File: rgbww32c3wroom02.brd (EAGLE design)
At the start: 36.8 x 20.3 mm, 25 parts

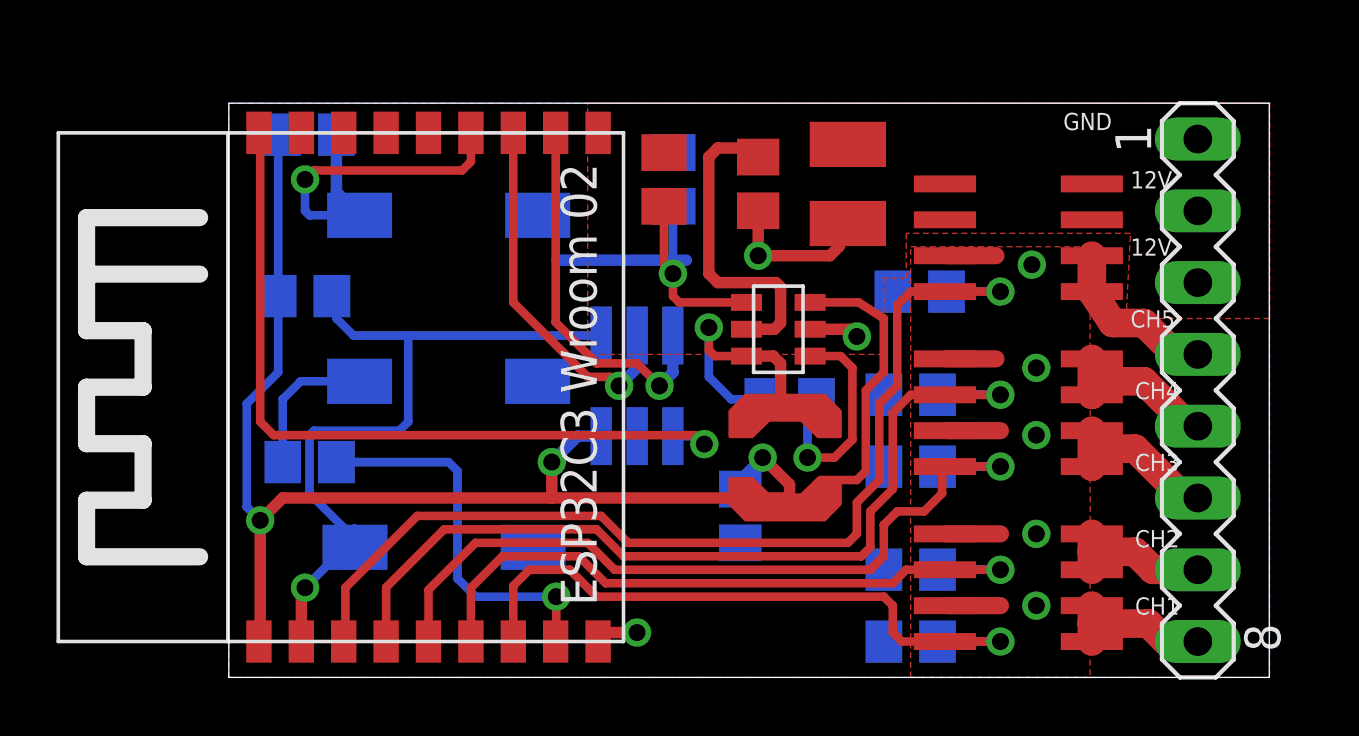
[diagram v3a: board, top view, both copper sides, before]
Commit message: resolved two minor mistakes
The footprint for L1 still needs to get it's solder mask taken off.
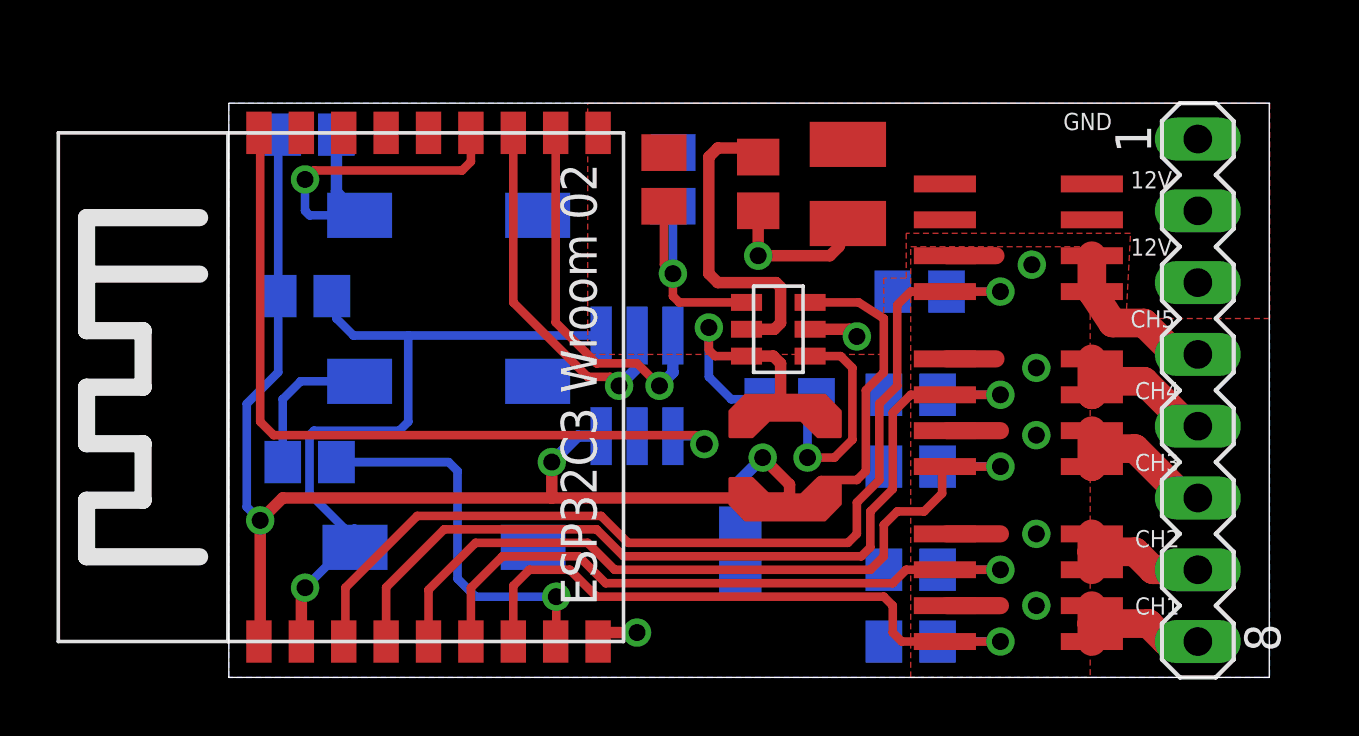
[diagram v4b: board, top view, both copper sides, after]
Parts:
- moved C5 1.27 mm to (18.1, 64.1)
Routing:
- net GND: track 22.5 -> 17.9 mm
- net 3V3: track 56.4 -> 57.7 mm
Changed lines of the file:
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@@
 <attribute name="VALUE" x="18.25625" y="78.58125" size="1.27" layer="28" rot="MR270"/>
 </element>
-<element name="C5" library="rcl" package="C0805" value="22µF" x="18.0975" y="65.405" smashed="yes" rot="MR270"/>
+<element name="C5" library="rcl" package="C0805" value="22µF" x="18.0975" y="64.135" smashed="yes" rot="MR270"/>
 <element name="C6" library="rcl" package="C0805" value="100nF" x="19.84375" y="69.5325" smashed="yes" rot="MR0"/>
 <element name="L1" library="TI_Components" package="LPS4018" value="15µH" x="19.685" y="67.46875" rot="R270"/>
@@
 <wire x1="13.0675" y1="60.96" x2="13.385" y2="61.2775" width="0.4064" layer="1"/>
 <wire x1="13.385" y1="61.2775" x2="14.44625" y2="61.2775" width="0.4064" layer="1"/>
-<wire x1="11.6175" y1="74.45375" x2="16.1925" y2="74.45375" width="0.4064" layer="16"/>
 <polygon width="0.3048" layer="1">
 <vertex x="24.13" y="59.69"/>
@@
 <wire x1="20.955" y1="66.675" x2="20.32" y2="66.04" width="0.3048" layer="1"/>
 <wire x1="20.32" y1="66.04" x2="19.84375" y2="66.04" width="0.3048" layer="1"/>
-<wire x1="18.0975" y1="66.355" x2="18.0975" y2="66.675" width="0.4064" layer="16"/>
+<wire x1="18.0975" y1="65.085" x2="18.0975" y2="66.675" width="0.4064" layer="16"/>
 <wire x1="18.0975" y1="66.675" x2="18.89125" y2="67.46875" width="0.4064" layer="16"/>
 <wire x1="19.84375" y1="66.04" x2="19.84375" y2="66.51625" width="0.4064" layer="1"/>
